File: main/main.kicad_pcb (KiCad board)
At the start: 2 copper layers, 45.1 x 52.6 mm, 37 parts, among them P2 CONN_5, P7 CONN_10, P8 CONN_7, U1 MKL17Z32VFM4, U4 ESD

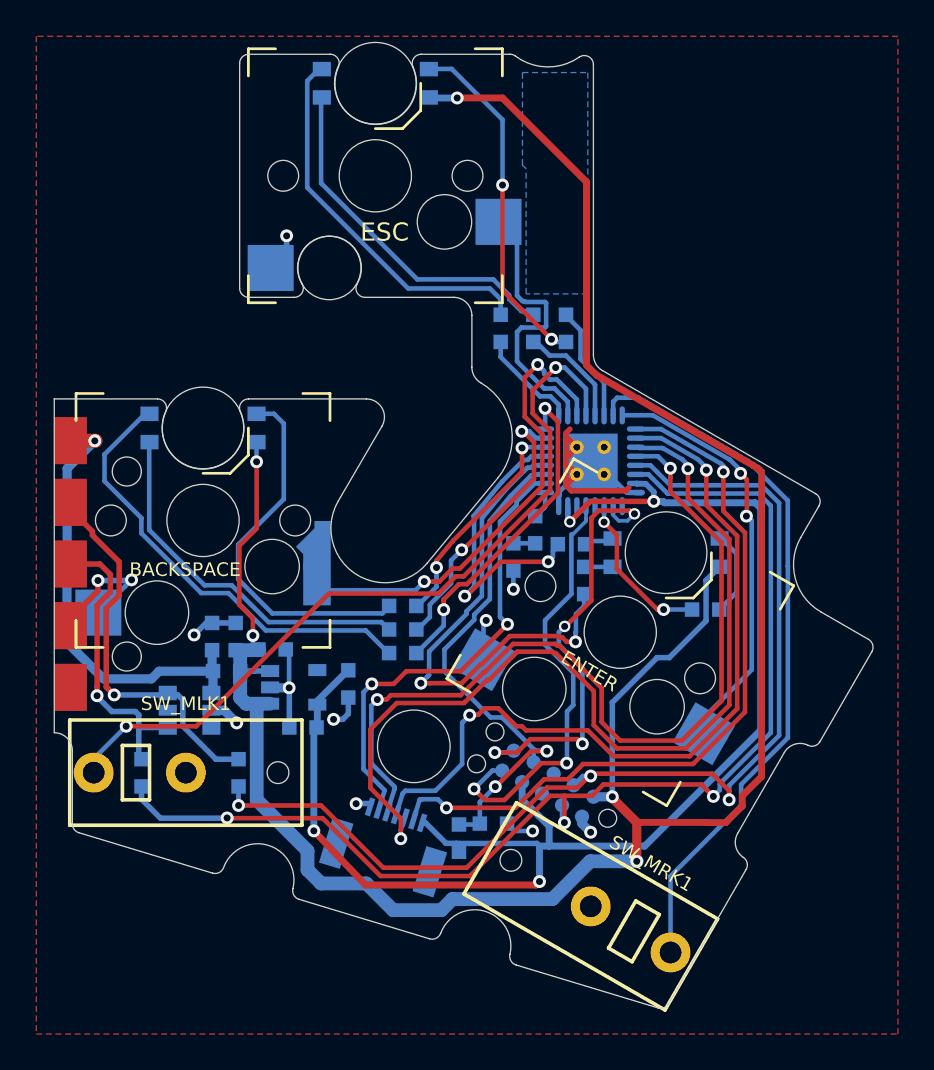
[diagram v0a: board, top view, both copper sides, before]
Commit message: Update microswitch modules.
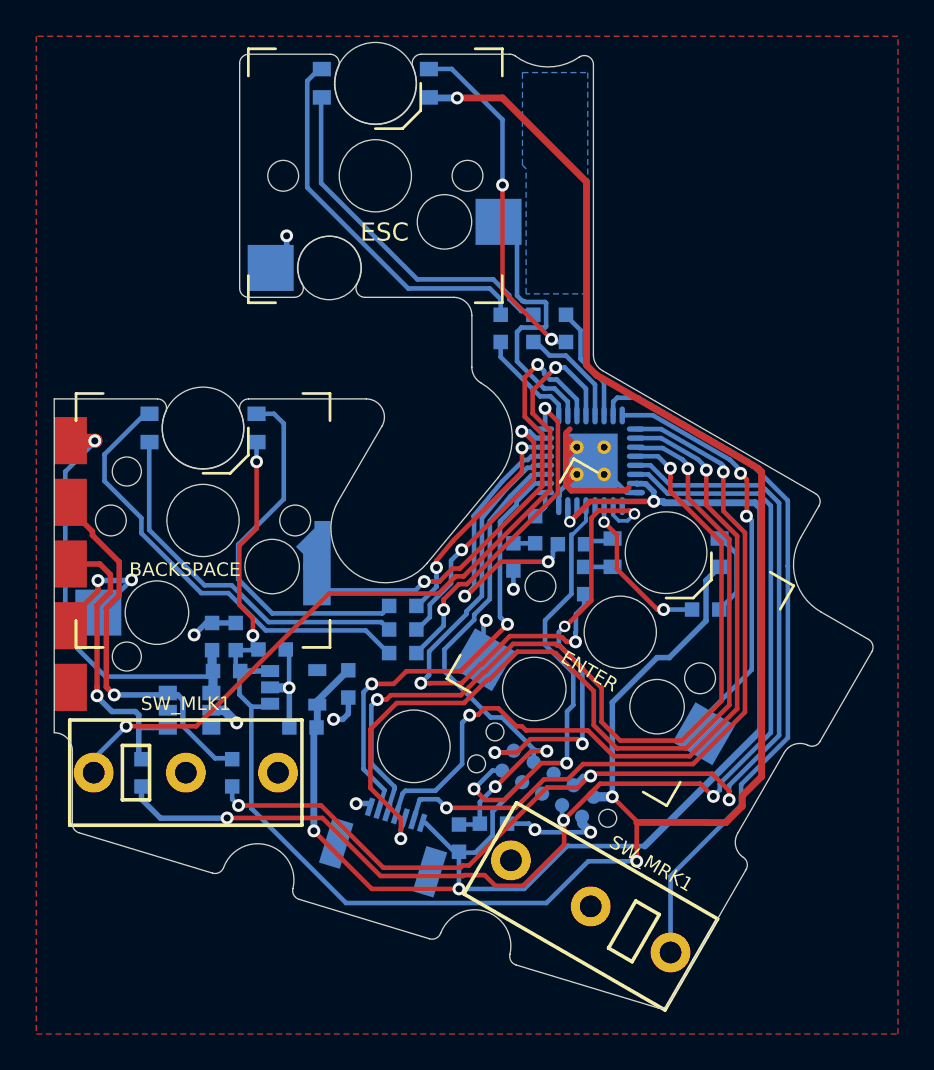
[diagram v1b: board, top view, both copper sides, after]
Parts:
- moved R6 0.35 mm to (134.8, 120.6)
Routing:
- net GND: track 43.2 -> 46.5 mm
- net +5V: track 129.8 -> 127.0 mm
- net +3V3: track 78.1 -> 75.5 mm

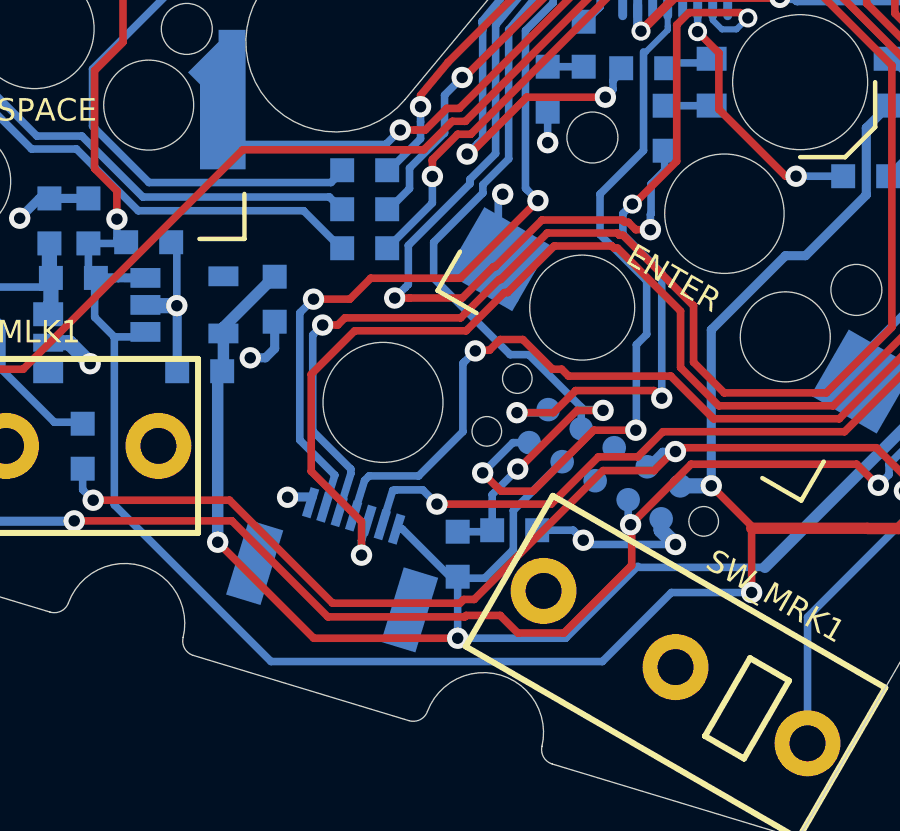
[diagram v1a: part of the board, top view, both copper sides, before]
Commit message: Move parts away from SW_MRK1 to ease hand its soldering.
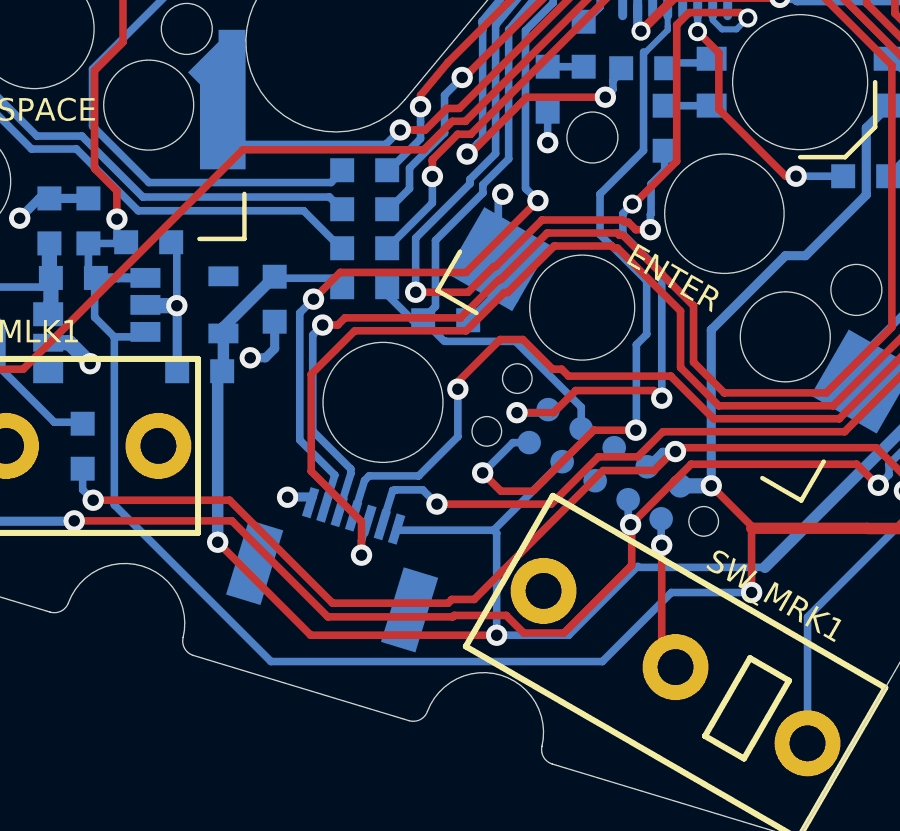
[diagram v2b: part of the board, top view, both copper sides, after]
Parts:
- moved R1 9.42 mm to (144.2, 115.3), turned to 0 degrees
- moved C3 7.37 mm to (146.9, 116.4)
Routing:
- net /RESET: track 29.4 -> 23.6 mm, vias 2 -> 0
- net +3V3: track 75.5 -> 77.3 mm
- net /TPM1_CH0: track 27.8 -> 26.6 mm
- net GND: track 46.5 -> 46.1 mm, vias 12 -> 11

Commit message: Optimize routing.
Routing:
- net +3V3: track 77.3 -> 67.5 mm, vias 4 -> 2
- net /SCL: track 64.4 -> 62.3 mm
- net /SDA: track 59.9 -> 59.1 mm
- net /SWDIO: track 24.1 -> 23.6 mm

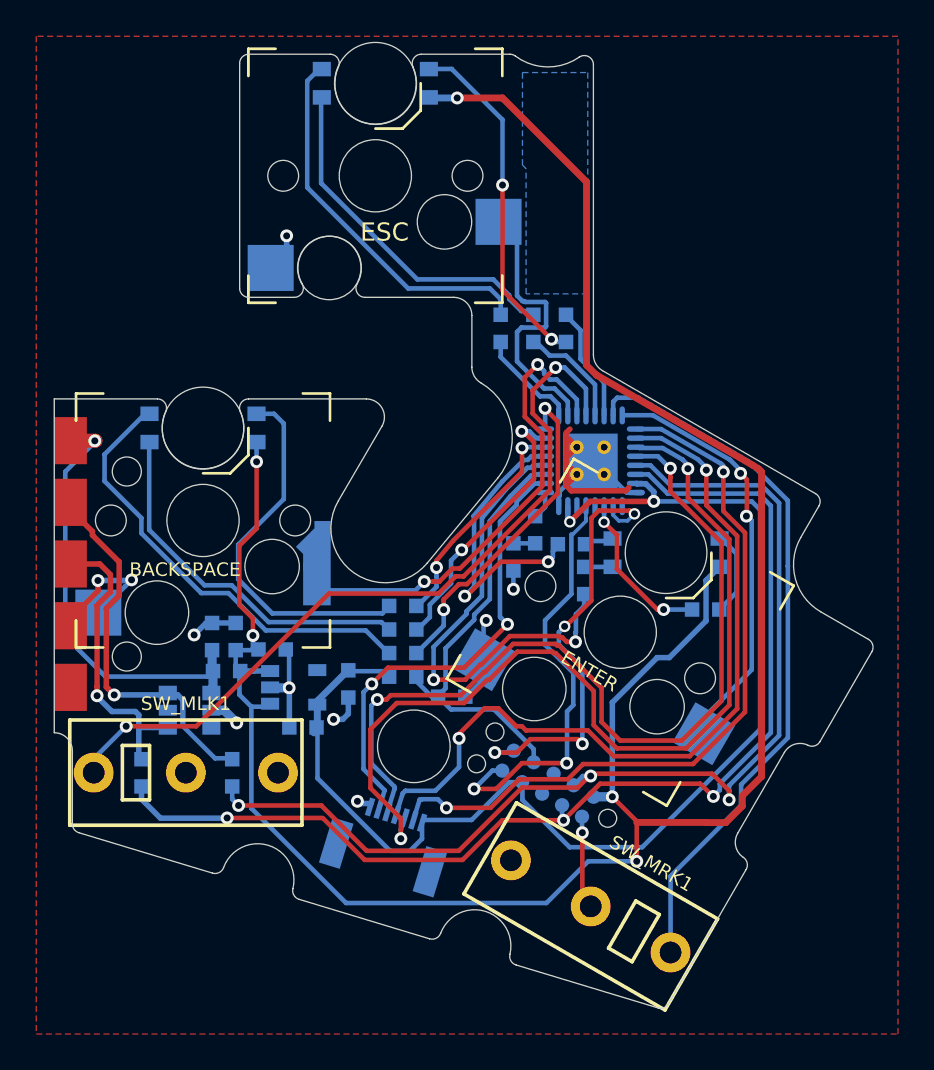
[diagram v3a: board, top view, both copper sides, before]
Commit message: Move components away from SW_MLK1 for easier solderability.
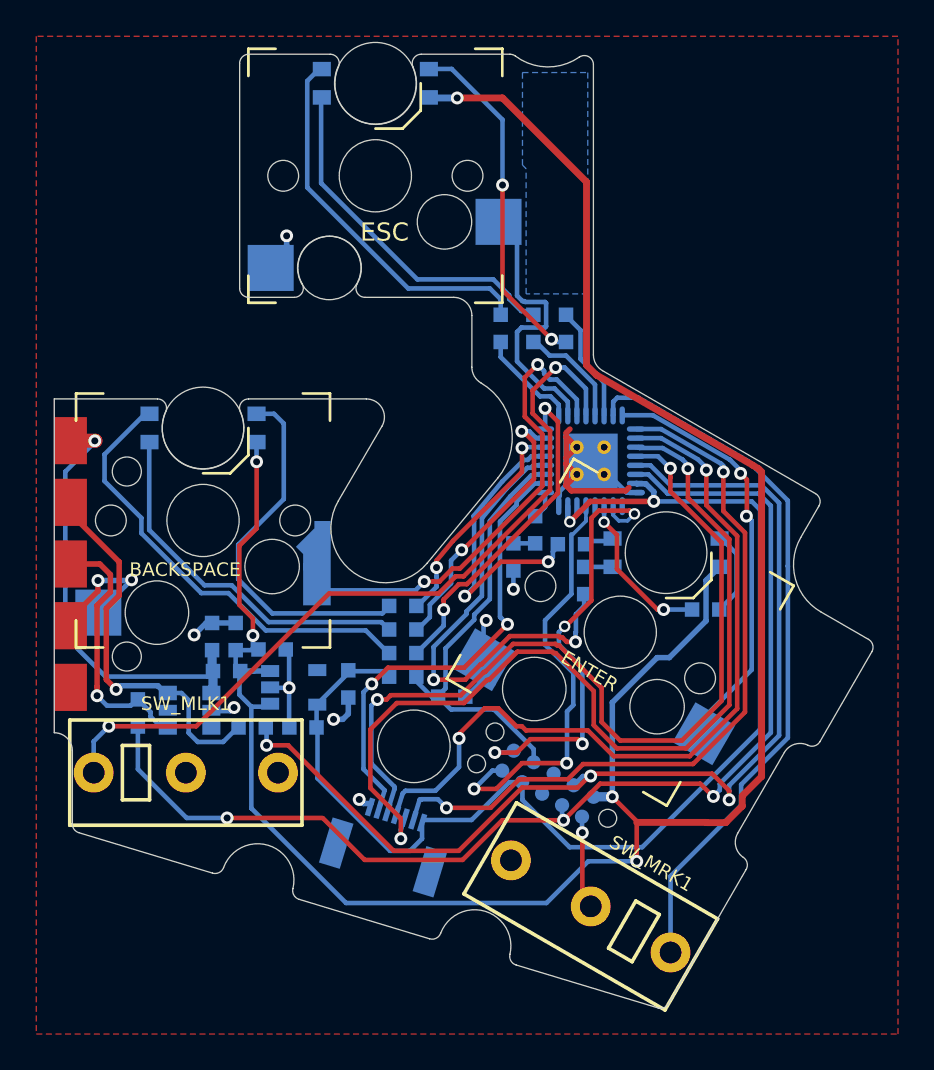
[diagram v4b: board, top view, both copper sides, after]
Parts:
- moved R7 3.31 mm to (129.6, 117.3)
- moved R6 2.73 mm to (135.9, 118.1), turned to 180 degrees
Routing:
- net /SCL: track 62.3 -> 64.7 mm
- net /SCL_BOTTOM: track 16.2 -> 13.9 mm
- net GND: track 46.1 -> 45.3 mm
- net +3V3: track 67.5 -> 66.9 mm
- net /KEY_MLEFT: track 43.4 -> 43.9 mm

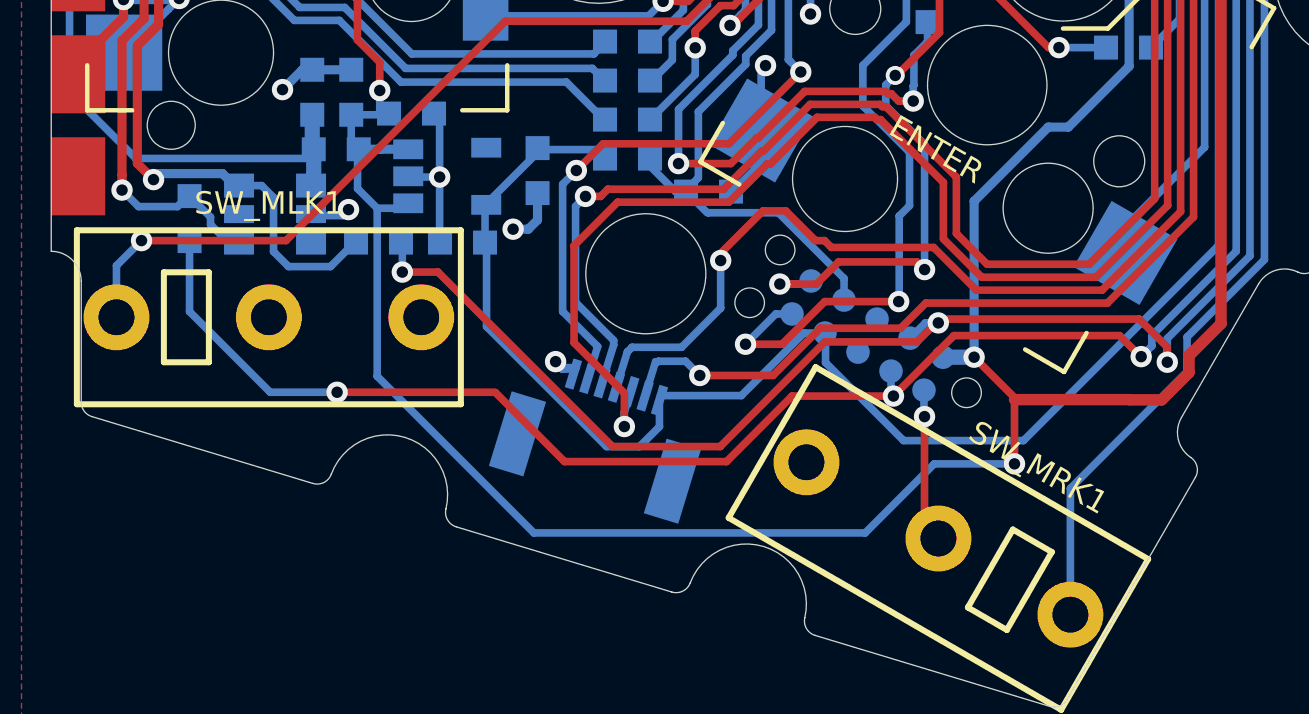
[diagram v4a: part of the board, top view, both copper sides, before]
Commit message: Simplify switch naming to SW1-SW6.
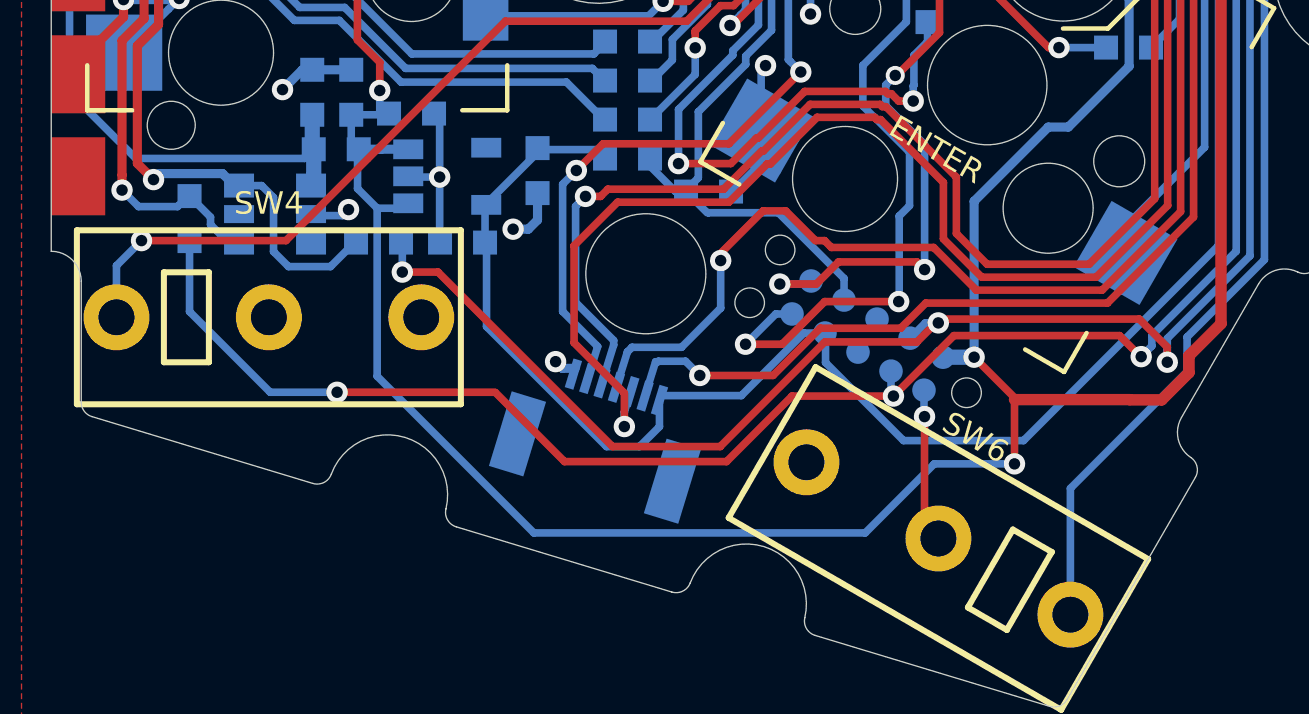
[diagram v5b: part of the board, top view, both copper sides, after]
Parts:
- renumbered D_TK1 to D1, D_LK1 to D2, D_RK1 to D3, D2 to D7, SW_TK1 to SW1, SW_LK1 to SW2, SW_RK1 to SW3, SW_MLK1 to SW4, SW_MRK1 to SW6
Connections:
- net /KEY_LEFT renamed /SW2
- net /KEY_MLEFT renamed /SW4
- net /KEY_MRIGHT renamed /SW6
- net /KEY_RIGHT renamed /SW3
- net /KEY_TOP renamed /SW1
- net /TB_BTN renamed /SW5

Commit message: Clean up silk screen.
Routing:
- net GND: track 45.3 -> 44.1 mm

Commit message: Bump version to 2.2.0
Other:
- board text added: "PCB ID: keycluster_main_2.2.0"
- board text removed: "PCB ID: keycluster_main_2.1.0"
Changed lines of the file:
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@@
   (title_block
     (title "UHK Key Cluster Module - Main Board")
-    (rev 2.1.0)
+    (rev 2.2.0)
     (company "Ultimate Gadget Laboratories Kft.")
   )
@@
     (effects (font (size 0.75 0.75) (thickness 0.15)) (justify mirror))
   )
-  (gr_text "PCB ID:\nkeycluster_main_2.1.0" (at 162.493312 121.437542 60) (layer B.SilkS)
+  (gr_text "PCB ID:\nkeycluster_main_2.2.0" (at 162.493312 121.437542 60) (layer B.SilkS)
     (effects (font (size 0.75 0.75) (thickness 0.15)) (justify mirror))
   )
